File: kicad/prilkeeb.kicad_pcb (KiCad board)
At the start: 2 copper layers, 176.1 x 130.6 mm, 76 parts, among them SW1 SW_SPDT, U2 Nice_Nano_V2

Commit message: Routing cont
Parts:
- moved D32 7.91 mm to (118.1, 136.5)
- moved D33 5.00 mm to (118.1, 132.5)
- moved D34 4.85 mm to (118.1, 128.5)
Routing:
- net Net-(D34-A): track 0.00 -> 73.2 mm
- net Net-(D33-A): track 0.00 -> 45.1 mm
- net Net-(D32-A): track 29.7 -> 14.6 mm
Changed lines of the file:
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@@
 	(footprint "ScottoKeebs_Components:Diode_DO-35"
 		(layer "B.Cu")
-		(at 118.11 133.35 180)
+		(at 118.12 128.5 180)
 		(descr "Diode, DO-35_SOD27 series, Axial, Horizontal, pin pitch=7.62mm, , length*diameter=4*2mm^2, , http://www.diodes.com/_files/packages/DO-35.pdf")
 		(tags "Diode DO-35_SOD27 series Axial Horizontal pin pitch 7.62mm  length 4mm diameter 2mm")
@@
 	(footprint "ScottoKeebs_Components:Diode_DO-35"
 		(layer "B.Cu")
-		(at 118.11 128.5875 180)
+		(at 118.12 136.5 180)
 		(descr "Diode, DO-35_SOD27 series, Axial, Horizontal, pin pitch=7.62mm, , length*diameter=4*2mm^2, , http://www.diodes.com/_files/packages/DO-35.pdf")
 		(tags "Diode DO-35_SOD27 series Axial Horizontal pin pitch 7.62mm  length 4mm diameter 2mm")
@@
 	(footprint "ScottoKeebs_Components:Diode_DO-35"
 		(layer "B.Cu")
-		(at 118.11 137.5 180)
+		(at 118.12 132.5 180)
 		(descr "Diode, DO-35_SOD27 series, Axial, Horizontal, pin pitch=7.62mm, , length*diameter=4*2mm^2, , http://www.diodes.com/_files/packages/DO-35.pdf")
 		(tags "Diode DO-35_SOD27 series Axial Horizontal pin pitch 7.62mm  length 4mm diameter 2mm")
@@
 	)
 	(segment
-		(start 118.11 137.5)
-		(end 119.61 136)
+		(start 104.774998 148.225002)
+		(end 116.5 136.5)
 		(width 0.2)
 		(layer "F.Cu")
@@
 	)
 	(segment
-		(start 118.11 137.5)
-		(end 118.11 133.35)
+		(start 118.12 128.5)
+		(end 118.12 132.5)
 		(width 0.2)
 		(layer "F.Cu")
@@
 	)
 	(segment
-		(start 177.12 136)
-		(end 179.12 138)
+		(start 116.5 136.5)
+		(end 118.12 136.5)
 		(width 0.2)
 		(layer "F.Cu")
@@
 	)
 	(segment
-		(start 104.774998 150.495001)
-		(end 105.114999 150.495001)
+		(start 118.12 136.5)
+		(end 118.62 136)
 		(width 0.2)
 		(layer "F.Cu")
@@
 	)
 	(segment
-		(start 119.61 136)
+		(start 118.62 136)
 		(end 177.12 136)
 		(width 0.2)
@@
 	)
 	(segment
-		(start 105.114999 150.495001)
-		(end 118.11 137.5)
+		(start 104.774998 150.495001)
+		(end 104.774998 148.225002)
 		(width 0.2)
 		(layer "F.Cu")
@@
 	)
 	(segment
-		(start 85.724998 150.495001)
-		(end 104.774998 150.495001)
+		(start 177.12 136)
+		(end 179.12 138)
 		(width 0.2)
 		(layer "F.Cu")
@@
 	)
 	(segment
-		(start 85.719999 150.5)
-		(end 85.724998 150.495001)
+		(start 118.12 132.5)
+		(end 118.12 136.5)
 		(width 0.2)
 		(layer "F.Cu")
@@
 	)
 	(segment
-		(start 118.11 133.35)
-		(end 118.11 128.5875)
+		(start 85.724998 150.495001)
+		(end 104.774998 150.495001)
+		(width 0.2)
+		(layer "F.Cu")
+		(net 33)
+	)
+	(segment
+		(start 85.719999 150.5)
+		(end 85.724998 150.495001)
 		(width 0.2)
 		(layer "F.Cu")
@@
 	)
 	(segment
-		(start 110.4125 128.5875)
-		(end 110.49 128.5875)
+		(start 119.062038 145.062038)
+		(end 110.5 136.5)
 		(width 0.2)
 		(layer "B.Cu")
@@
 	(segment
 		(start 121.571192 145.062038)
-		(end 112.562038 145.062038)
+		(end 119.062038 145.062038)
 		(width 0.2)
 		(layer "B.Cu")
@@
 	)
 	(segment
-		(start 106.5 139)
-		(end 106.5 132.5)
+		(start 121 152)
+		(end 109 140)
 		(width 0.2)
 		(layer "B.Cu")
-		(net 37)
+		(net 38)
 	)
 	(segment
-		(start 112.562038 145.062038)
-		(end 106.5 139)
+		(start 137.725976 152)
+		(end 121 152)
 		(width 0.2)
 		(layer "B.Cu")
-		(net 37)
+		(net 38)
 	)
 	(segment
-		(start 106.5 132.5)
-		(end 110.4125 128.5875)
+		(start 140.055325 149.670651)
+		(end 137.725976 152)
 		(width 0.2)
 		(layer "B.Cu")
-		(net 37)
+		(net 38)
+	)
+	(segment
+		(start 109 140)
+		(end 109 134)
+		(width 0.2)
+		(layer "B.Cu")
+		(net 38)
+	)
+	(segment
+		(start 109 134)
+		(end 110.5 132.5)
+		(width 0.2)
+		(layer "B.Cu")
+		(net 38)
+	)
+	(segment
+		(start 158.539459 154.279263)
+		(end 155.818722 157)
+		(width 0.2)
+		(layer "B.Cu")
+		(net 39)
+	)
+	(segment
+		(start 123 157)
+		(end 107 141)
+		(width 0.2)
+		(layer "B.Cu")
+		(net 39)
+	)
+	(segment
+		(start 107 132)
+		(end 110.5 128.5)
+		(width 0.2)
+		(layer "B.Cu")
+		(net 39)
+	)
+	(segment
+		(start 107 141)
+		(end 107 132)
+		(width 0.2)
+		(layer "B.Cu")
+		(net 39)
+	)
+	(segment
+		(start 155.818722 157)
+		(end 123 157)
+		(width 0.2)
+		(layer "B.Cu")
+		(net 39)
 	)
 	(segment

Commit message: Update components
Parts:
- added RST_SW2: SW_Push, ScottoKeebs_Components:Button_TL3342, B.Cu at (188.5, 113.5)
- ROT1: footprint ScottoKeebs_Scotto:Encoder_EC11_MX -> prillkeeb:Encoder_EC11_MX_Jumpers_Reversible
- RST_SW1: footprint Button_Switch_THT:SW_PUSH_6mm_H4.3mm -> ScottoKeebs_Components:Button_TL3342
- moved RST_SW1 22.3 mm to (188.5, 113.5)
- moved SW1 20.7 mm to (201.5, 113.5)
- moved ROT1 9.56 mm to (193.5, 98.6)
- moved U2 2.65 mm to (193.5, 70.6)
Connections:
- U2 pad 24: (no net) -> unconnected-(U2-B+-Pad24)
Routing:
- net Col_5: track 63.2 -> 104.3 mm
- net Net-(DROTARY1-A): track 0.00 -> 13.4 mm

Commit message: Routing
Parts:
- ROT1: moved to F.Cu
- moved SW1 21.5 mm to (201.5, 92.0)
- moved RST_SW1 20.0 mm to (188.5, 93.5)
- moved RST_SW2 20.0 mm to (188.5, 93.5)
- moved ROT1 8.40 mm to (193.5, 107.0), turned to -90 degrees
- moved D14 6.24 mm to (172.9, 95.2)
- moved D21 6.24 mm to (172.9, 114.3)
- moved D28 6.24 mm to (172.9, 133.3)
- moved D7 6.24 mm to (172.9, 76.2)
- moved DROTARY1 6.24 mm to (172.9, 138.0)
- moved BT1 2.40 mm to (193.0, 64.5)
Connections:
- ROT1 pad C: unconnected-(ROT1-PadC) -> GND
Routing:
- net Col_1: track 87.5 -> 249.5 mm, vias 0 -> 1
- net Col_2: track 82.9 -> 216.2 mm, vias 0 -> 1
- net Col_3: track 92.2 -> 206.9 mm, vias 0 -> 2
- net Col_4: track 104.9 -> 194.8 mm, vias 0 -> 2
- net Col_5: track 104.3 -> 176.7 mm, vias 0 -> 2
- net Col_6: track 108.6 -> 178.2 mm, vias 0 -> 1
- net Col_7: track 65.3 -> 132.5 mm, vias 0 -> 1
- net Row_5: track 128.6 -> 190.1 mm, vias 0 -> 2
- net Row_4: track 139.9 -> 200.2 mm, vias 0 -> 2
- net RST: track 0.00 -> 57.6 mm, vias 0 -> 1
- net Net-(DROTARY1-A): track 13.4 -> 63.4 mm, vias 0 -> 1
- net Row_3: track 141.2 -> 184.7 mm, vias 0 -> 1
- net B+: track 0.00 -> 38.7 mm, vias 0 -> 1
- net RotaryA: track 0.00 -> 37.5 mm, vias 0 -> 1
- net Net-(BT1-+): track 0.00 -> 35.4 mm, vias 0 -> 1
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- added copper zone on B.Cu, net GND
- added copper zone on F.Cu, net GND

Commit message: Update edgecut
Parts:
- moved SW1 30.6 mm to (193.5, 121.5), turned to 0 degrees
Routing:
- net B+: track 38.7 -> 74.5 mm
- net Net-(BT1-+): track 35.4 -> 67.0 mm
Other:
- board size 176.1 x 130.6 mm -> 171.1 x 130.6 mm

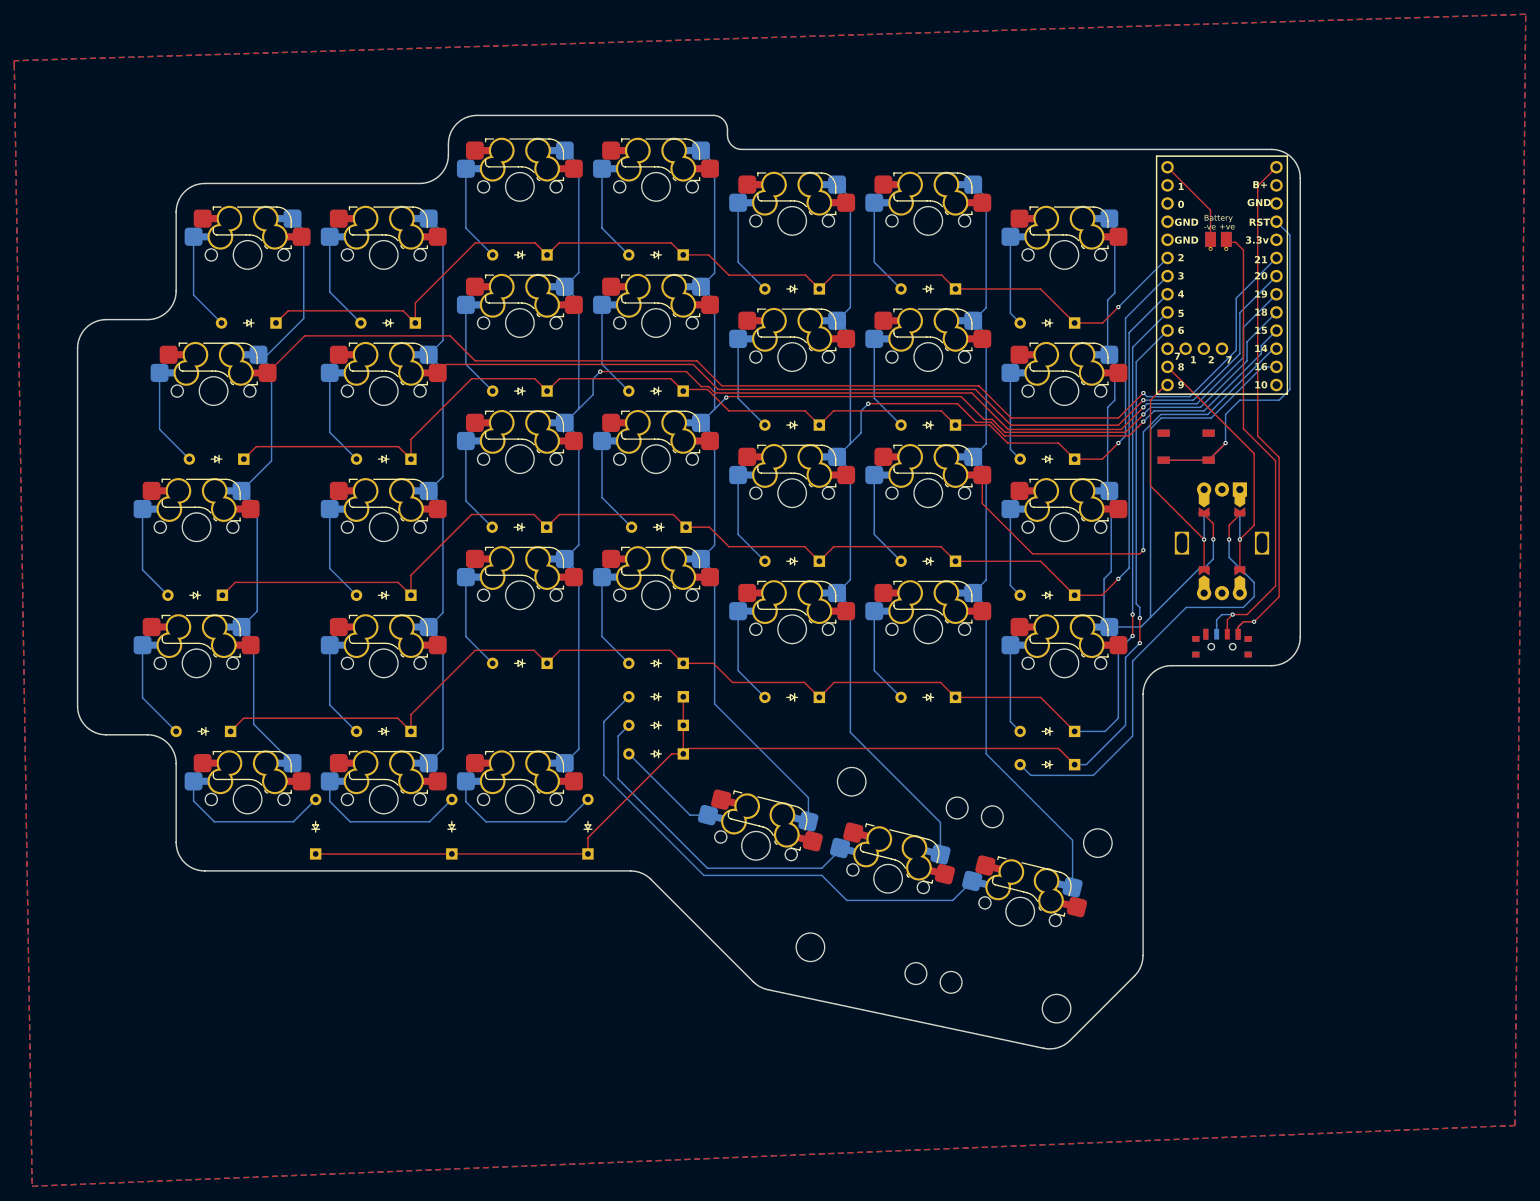
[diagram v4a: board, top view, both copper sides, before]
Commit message: Update diode type
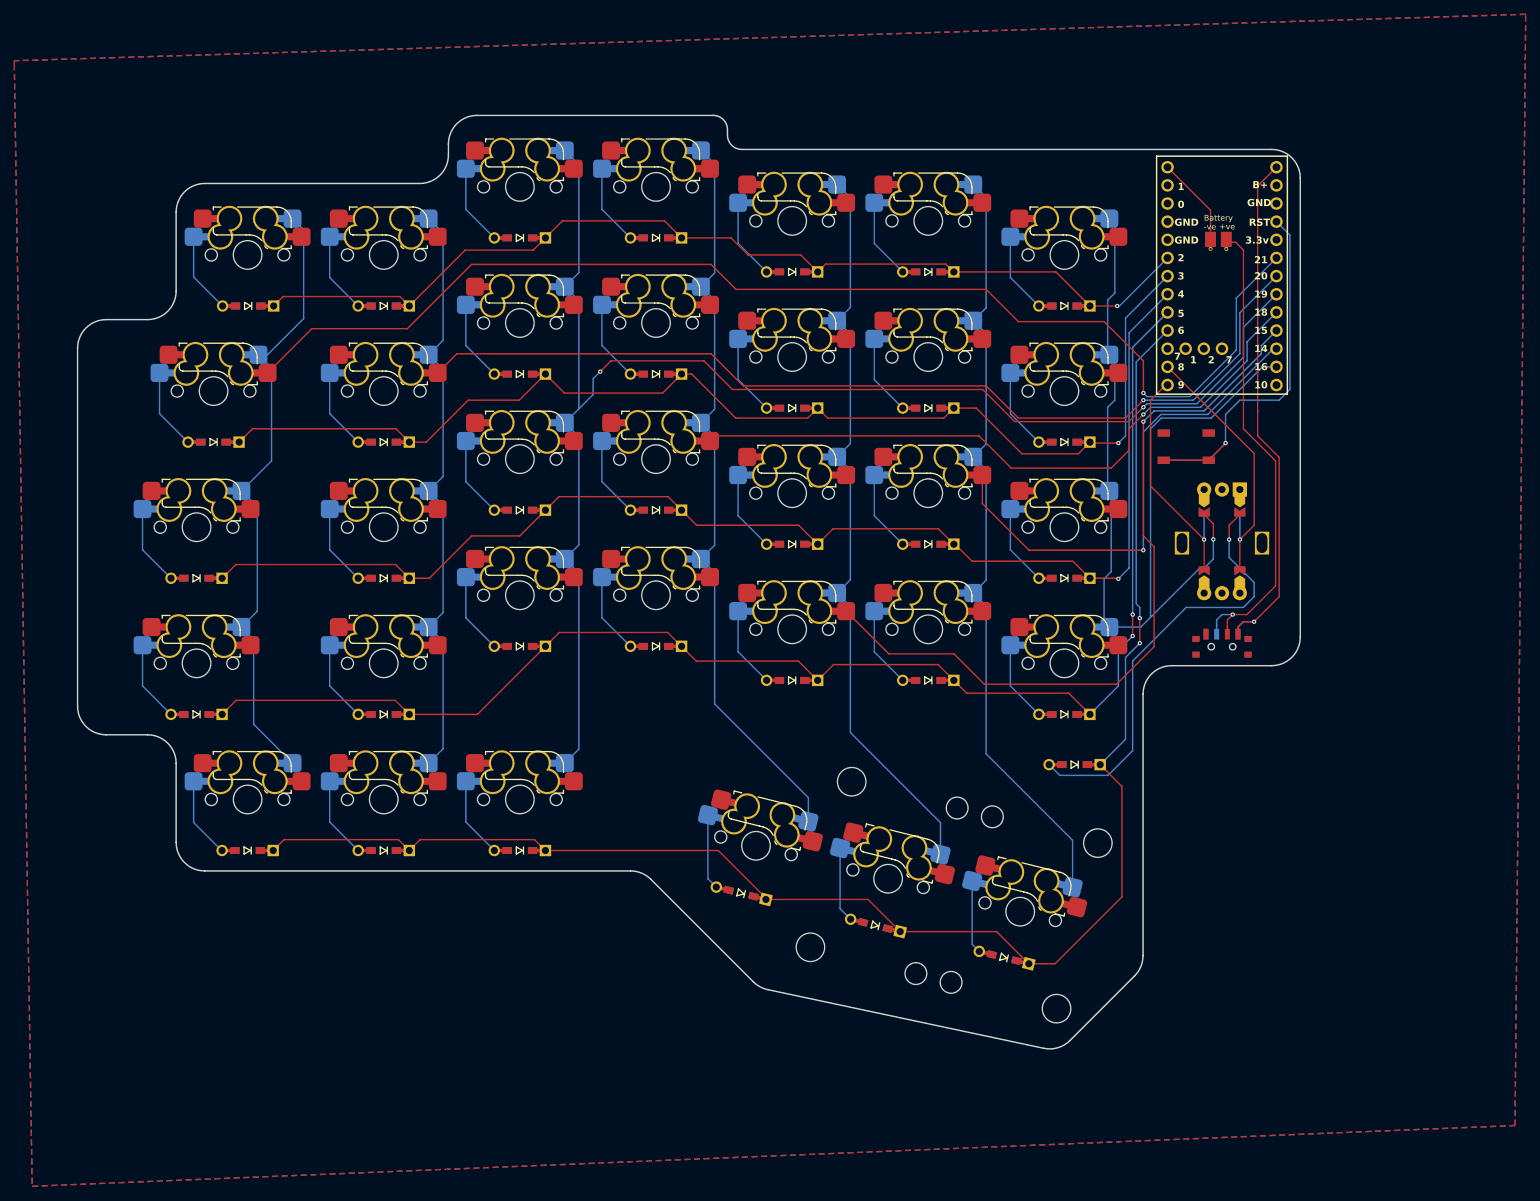
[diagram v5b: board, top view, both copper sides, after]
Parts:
- D1, D10, D11, D12, D13, D14, D15, D16, D17, D18, D19, D2, D20, D21, D22, D23, D24, D25, D26, D27, D28, D29, D3, D30, D31, D32, D33, D34, D4, D5, D6, D7, D8, D9, DROTARY1: footprint ScottoKeebs_Components:Diode_DO-35 -> dumta:D_SMD_TH
- moved D34 57.8 mm to (163.0, 165.0), turned to 166 degrees
- moved D33 38.8 mm to (145.0, 160.5), turned to 166 degrees
- moved D32 21.1 mm to (126.2, 156.0), turned to 166 degrees
- moved D29 9.54 mm to (57.1, 150.0), turned to 180 degrees
- moved D30 9.54 mm to (76.2, 150.0), turned to 180 degrees
- moved D31 9.54 mm to (95.2, 150.0), turned to 180 degrees
- moved D22 5.32 mm to (50.0, 131.0)
- moved D2 5.02 mm to (76.2, 73.8)
- moved D8 4.86 mm to (52.4, 92.9)
- moved D18 4.83 mm to (114.3, 102.4)
- moved D1 4.57 mm to (57.2, 73.8)
- moved D24 4.49 mm to (95.2, 121.4)
- moved D25 4.49 mm to (114.3, 121.4)
- moved D26 4.49 mm to (133.3, 126.2)
- moved D27 4.49 mm to (152.4, 126.2)
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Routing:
- net Net-(D34-A): track 72.4 -> 10.3 mm
- net Net-(D33-A): track 45.7 -> 10.6 mm
- net Col_5: track 176.7 -> 210.5 mm, vias 2 -> 1
- net Row_5: track 190.1 -> 216.7 mm
- net Net-(D31-A): track 22.4 -> 11.3 mm
- net Net-(D30-A): track 22.4 -> 11.3 mm
- net Net-(D29-A): track 22.3 -> 11.4 mm
- net Col_1: track 249.5 -> 257.5 mm
- net Row_4: track 200.2 -> 195.1 mm
- net Net-(D32-A): track 14.6 -> 10.6 mm
- net Col_4: track 194.8 -> 198.6 mm, vias 2 -> 1
- net Row_3: track 184.7 -> 181.0 mm
- net Net-(DROTARY1-A): track 63.4 -> 60.6 mm
- net Row_1: track 143.9 -> 141.1 mm
- net Net-(D22-A): track 14.0 -> 11.3 mm
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
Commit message: Mounting holes
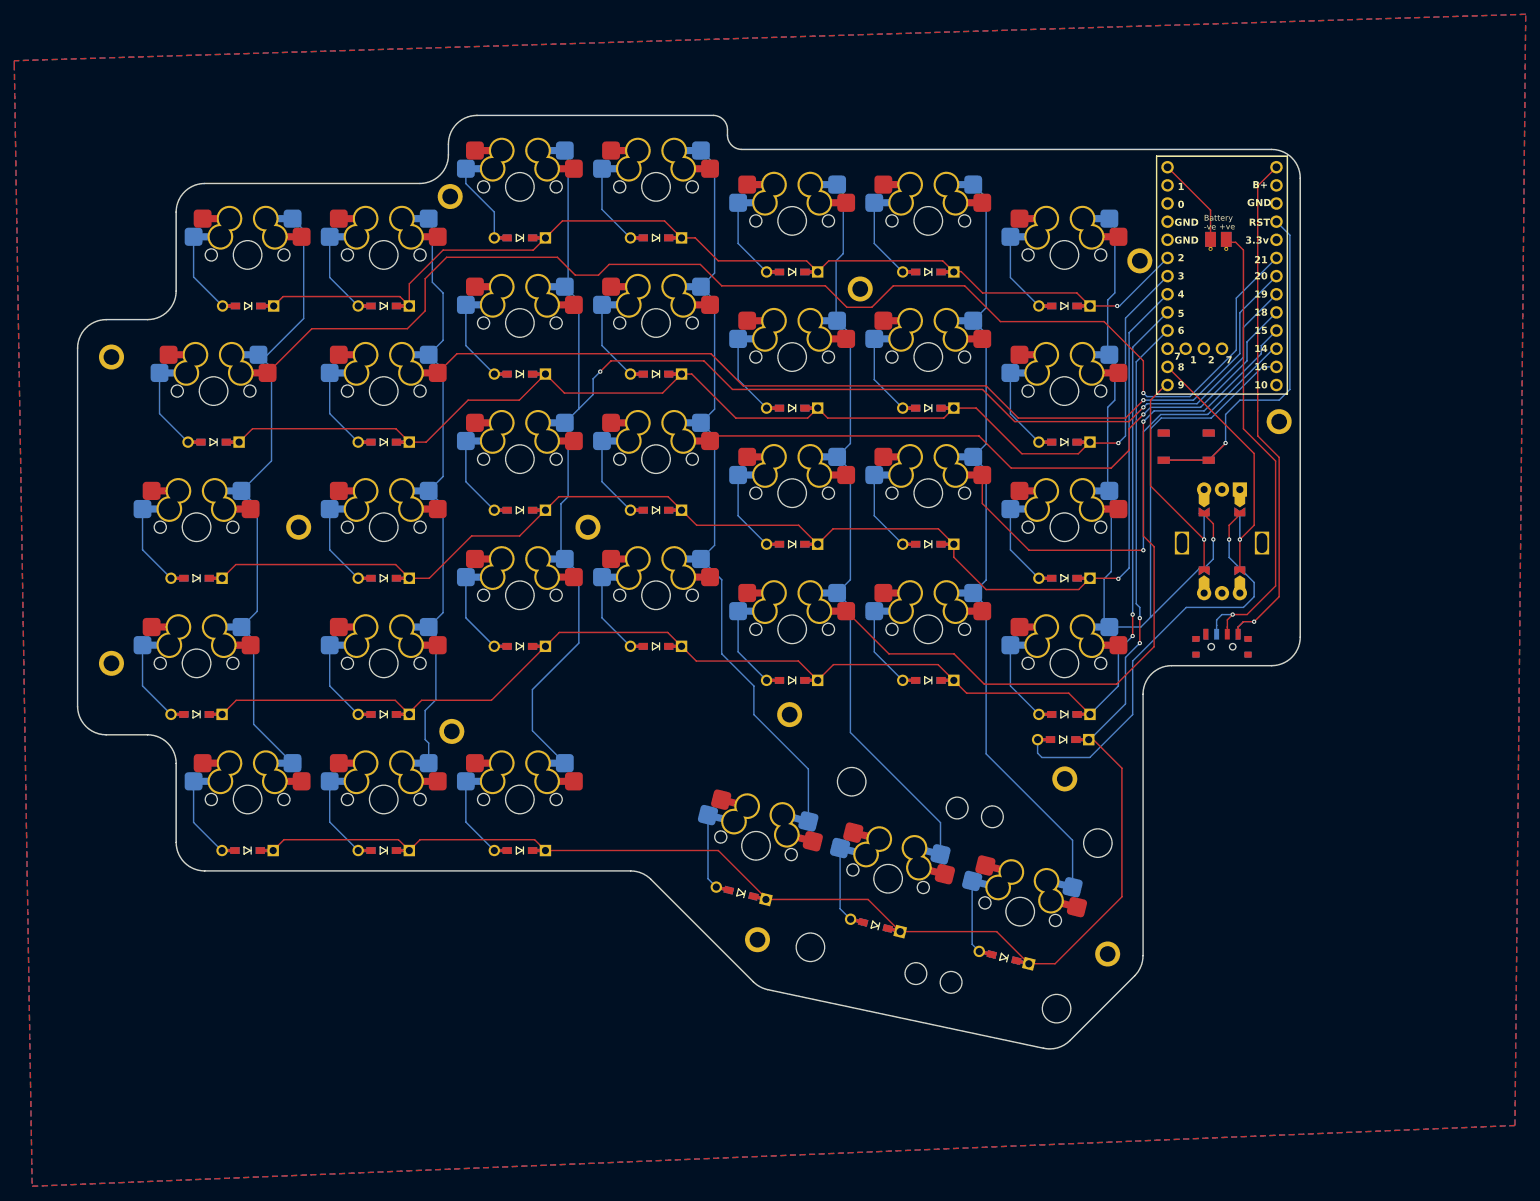
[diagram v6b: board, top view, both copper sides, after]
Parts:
- added Ref**: Val**, swoop:M2_hole_3.5mm, F.Cu at (38.1, 123.8)
- added Ref**: Val**, swoop:M2_hole_3.5mm, F.Cu at (133.0, 131.0)
- added Ref**: Val**, swoop:M2_hole_3.5mm, F.Cu at (201.5, 90.0)
- added Ref**: Val**, swoop:M2_hole_3.5mm, F.Cu at (104.8, 104.8)
- added Ref**: Val**, swoop:M2_hole_3.5mm, F.Cu at (38.1, 81.0)
- added Ref**: Val**, swoop:M2_hole_3.5mm, F.Cu at (85.7, 133.3)
- added Ref**: Val**, swoop:M2_hole_3.5mm, F.Cu at (177.5, 164.5)
- added Ref**: Val**, swoop:M2_hole_3.5mm, F.Cu at (64.3, 104.8)
- added Ref**: Val**, swoop:M2_hole_3.5mm, F.Cu at (142.9, 71.4)
- added Ref**: Val**, swoop:M2_hole_3.5mm, F.Cu at (171.5, 140.0)
- added Ref**: Val**, swoop:M2_hole_3.5mm, F.Cu at (182.0, 67.5)
- added Ref**: Val**, swoop:M2_hole_3.5mm, F.Cu at (85.5, 58.5)
- added Ref**: Val**, swoop:M2_hole_3.5mm, F.Cu at (128.5, 162.5)
- moved DROTARY1 3.85 mm to (171.3, 134.5)
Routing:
- net Col_1: track 257.5 -> 264.7 mm
- net Row_3: track 181.0 -> 183.3 mm
- net Row_5: track 216.7 -> 218.5 mm
- net Col_3: track 207.3 -> 209.0 mm
- net Row_1: track 141.1 -> 142.0 mm
- net Net-(DROTARY1-A): track 60.6 -> 59.7 mm
- net Col_5: track 210.5 -> 209.8 mm

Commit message: Fix mounting holes
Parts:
- moved Ref** 12.0 mm to (181.5, 55.5)
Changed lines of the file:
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@@
 	(footprint "swoop:M2_hole_3.5mm"
 		(layer "F.Cu")
-		(at 182 67.5)
+		(at 181.5 55.5)
 		(descr "Mounting Hole 2.2mm, no annular, M2")
 		(tags "mounting hole 2.2mm no annular m2")
